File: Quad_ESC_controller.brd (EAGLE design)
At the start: 100 x 80 mm, 28 parts, among them IC1 OP-AMP, Y1 ECS-80-S-4X

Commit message: added test points
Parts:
- added J1, J2, J3, J4, J5, J6, J7, J8: (no value), SparkFun-Connectors:1X01
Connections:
- new net N$10: J1.1
- new net N$3: J4.1
- new net N$4: J5.1
- new net N$5: J6.1
- new net N$7: J7.1
- new net N$8: J3.1
- new net N$9: J2.1
- net N$6: now also J8.1
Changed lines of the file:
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@@
 <attribute name="VALUE" x="-70.485" y="3.175" size="1.27" layer="27" ratio="16" rot="R90"/>
+</element>
+<element name="J1" library="SparkFun-Connectors" library_urn="urn:adsk.eagle:library:513" package="1X01" package3d_urn="urn:adsk.eagle:package:38028/1" value="" x="-74.93" y="2.54" smashed="yes">
+<attribute name="NAME" x="-76.2" y="3.937" size="0.6096" layer="25" font="vector" ratio="20"/>
+<attribute name="VALUE" x="-76.2" y="1.016" size="0.6096" layer="27" font="vector" ratio="20" align="top-left"/>
+</element>
+<element name="J2" library="SparkFun-Connectors" library_urn="urn:adsk.eagle:library:513" package="1X01" package3d_urn="urn:adsk.eagle:package:38028/1" value="" x="-80.01" y="2.54" smashed="yes">
+<attribute name="NAME" x="-81.28" y="3.937" size="0.6096" layer="25" font="vector" ratio="20"/>
+<attribute name="VALUE" x="-81.28" y="1.016" size="0.6096" layer="27" font="vector" ratio="20" align="top-left"/>
+</element>
+<element name="J3" library="SparkFun-Connectors" library_urn="urn:adsk.eagle:library:513" package="1X01" package3d_urn="urn:adsk.eagle:package:38028/1" value="" x="-85.09" y="2.54" smashed="yes">
+<attribute name="NAME" x="-86.36" y="3.937" size="0.6096" layer="25" font="vector" ratio="20"/>
+<attribute name="VALUE" x="-86.36" y="1.016" size="0.6096" layer="27" font="vector" ratio="20" align="top-left"/>
+</element>
+<element name="J4" library="SparkFun-Connectors" library_urn="urn:adsk.eagle:library:513" package="1X01" package3d_urn="urn:adsk.eagle:package:38028/1" value="" x="-85.09" y="-2.54" smashed="yes">
+<attribute name="NAME" x="-86.36" y="-1.143" size="0.6096" layer="25" font="vector" ratio="20"/>
+<attribute name="VALUE" x="-86.36" y="-4.064" size="0.6096" layer="27" font="vector" ratio="20" align="top-left"/>
+</element>
+<element name="J5" library="SparkFun-Connectors" library_urn="urn:adsk.eagle:library:513" package="1X01" package3d_urn="urn:adsk.eagle:package:38028/1" value="" x="-81.28" y="-2.54" smashed="yes">
+<attribute name="NAME" x="-82.55" y="-1.143" size="0.6096" layer="25" font="vector" ratio="20"/>
+<attribute name="VALUE" x="-82.55" y="-4.064" size="0.6096" layer="27" font="vector" ratio="20" align="top-left"/>
+</element>
+<element name="J6" library="SparkFun-Connectors" library_urn="urn:adsk.eagle:library:513" package="1X01" package3d_urn="urn:adsk.eagle:package:38028/1" value="" x="-85.09" y="-6.35" smashed="yes">
+<attribute name="NAME" x="-86.36" y="-4.953" size="0.6096" layer="25" font="vector" ratio="20"/>
+<attribute name="VALUE" x="-86.36" y="-7.874" size="0.6096" layer="27" font="vector" ratio="20" align="top-left"/>
+</element>
+<element name="J7" library="SparkFun-Connectors" library_urn="urn:adsk.eagle:library:513" package="1X01" package3d_urn="urn:adsk.eagle:package:38028/1" value="" x="-85.09" y="-10.16" smashed="yes">
+<attribute name="NAME" x="-86.36" y="-8.763" size="0.6096" layer="25" font="vector" ratio="20"/>
+<attribute name="VALUE" x="-86.36" y="-11.684" size="0.6096" layer="27" font="vector" ratio="20" align="top-left"/>
+</element>
+<element name="J8" library="SparkFun-Connectors" library_urn="urn:adsk.eagle:library:513" package="1X01" package3d_urn="urn:adsk.eagle:package:38028/1" value="" x="-90.17" y="-8.89" smashed="yes">
+<attribute name="NAME" x="-91.44" y="-7.493" size="0.6096" layer="25" font="vector" ratio="20"/>
+<attribute name="VALUE" x="-91.44" y="-10.414" size="0.6096" layer="27" font="vector" ratio="20" align="top-left"/>
 </element>
 </elements>
@@
 <contactref element="R6" pad="1"/>
 <contactref element="OP-AMP1" pad="2"/>
+<contactref element="J8" pad="1"/>
+<wire x1="-59.055" y1="2.2225" x2="-90.17" y2="-8.89" width="0" layer="19" extent="1-1"/>
 <wire x1="-44.87" y1="67.31" x2="-59.055" y2="2.2225" width="0" layer="19" extent="1-1"/>
 <wire x1="-38.95" y1="67.31" x2="-44.87" y2="67.31" width="0" layer="19" extent="1-1"/>
 </signal>
+<signal name="N$3">
+<contactref element="J4" pad="1"/>
+</signal>
+<signal name="N$4">
+<contactref element="J5" pad="1"/>
+</signal>
+<signal name="N$5">
+<contactref element="J6" pad="1"/>
+</signal>
+<signal name="N$7">
+<contactref element="J7" pad="1"/>
+</signal>
+<signal name="N$8">
+<contactref element="J3" pad="1"/>
+</signal>
+<signal name="N$9">
+<contactref element="J2" pad="1"/>
+</signal>
+<signal name="N$10">
+<contactref element="J1" pad="1"/>
+</signal>
 </signals>

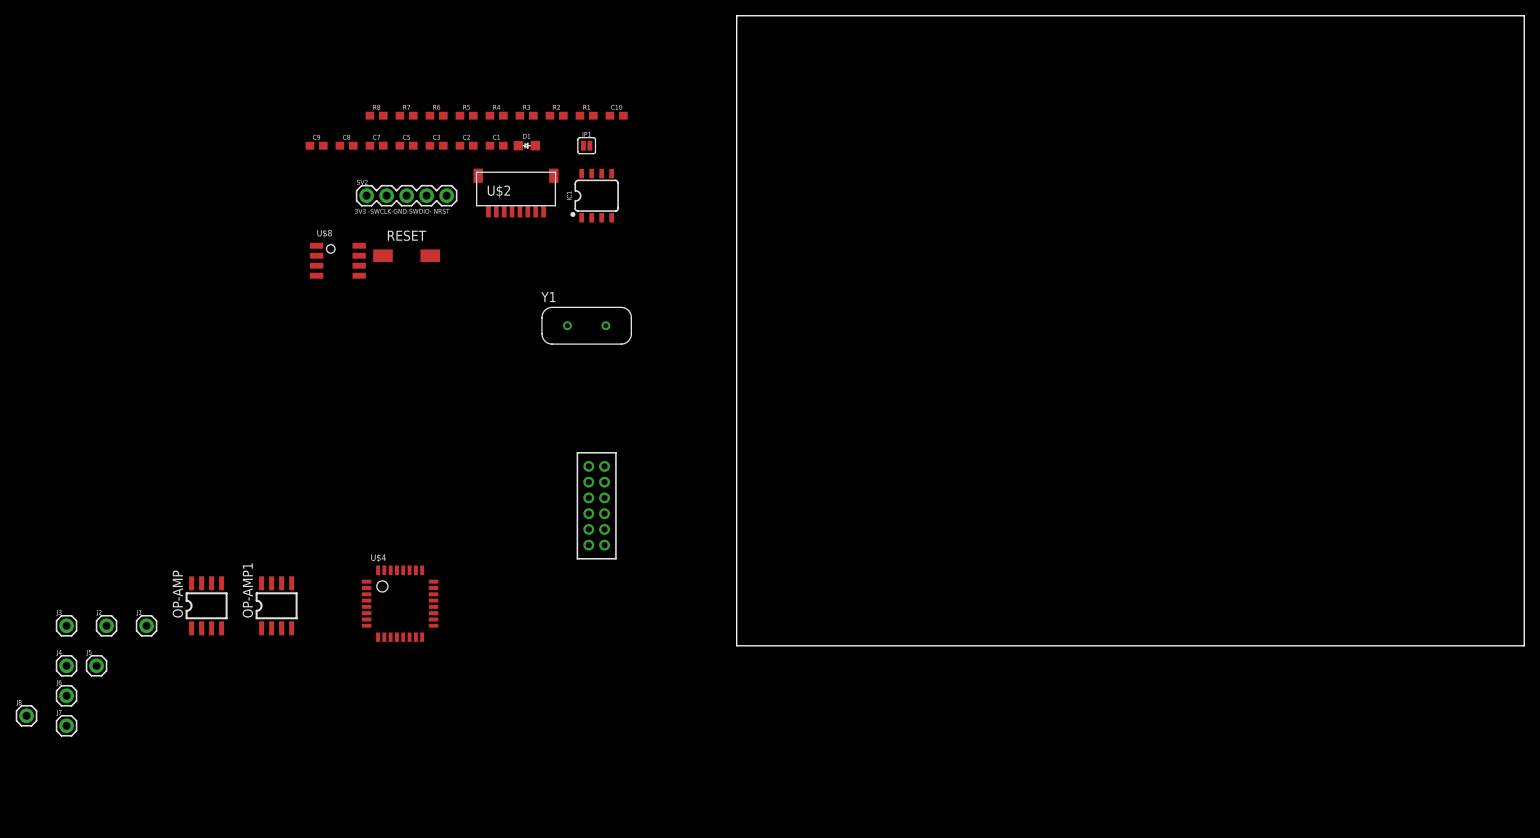
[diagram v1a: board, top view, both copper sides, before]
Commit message: add board size
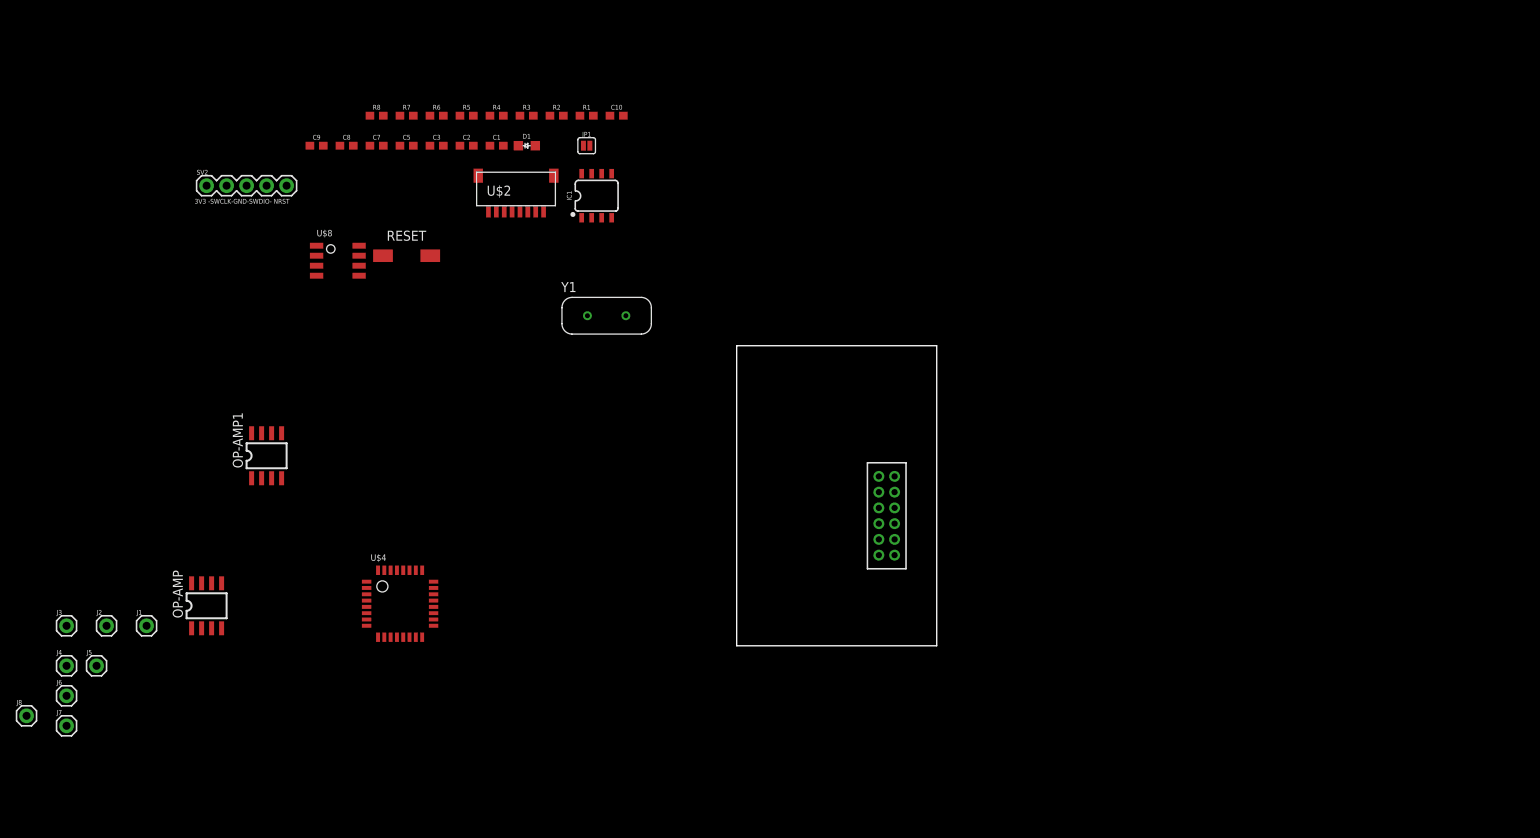
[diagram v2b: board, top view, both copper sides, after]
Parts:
- moved U$3 36.9 mm to (19.1, 16.5)
- moved SV2 20.4 mm to (-67.3, 58.4)
- moved OP-AMP1 19.1 mm to (-59.7, 24.1)
- moved Y1 2.84 mm to (-16.5, 41.9)
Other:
- board size 100 x 80 mm -> 25.4 x 38.1 mm

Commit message: Example placement for adapter
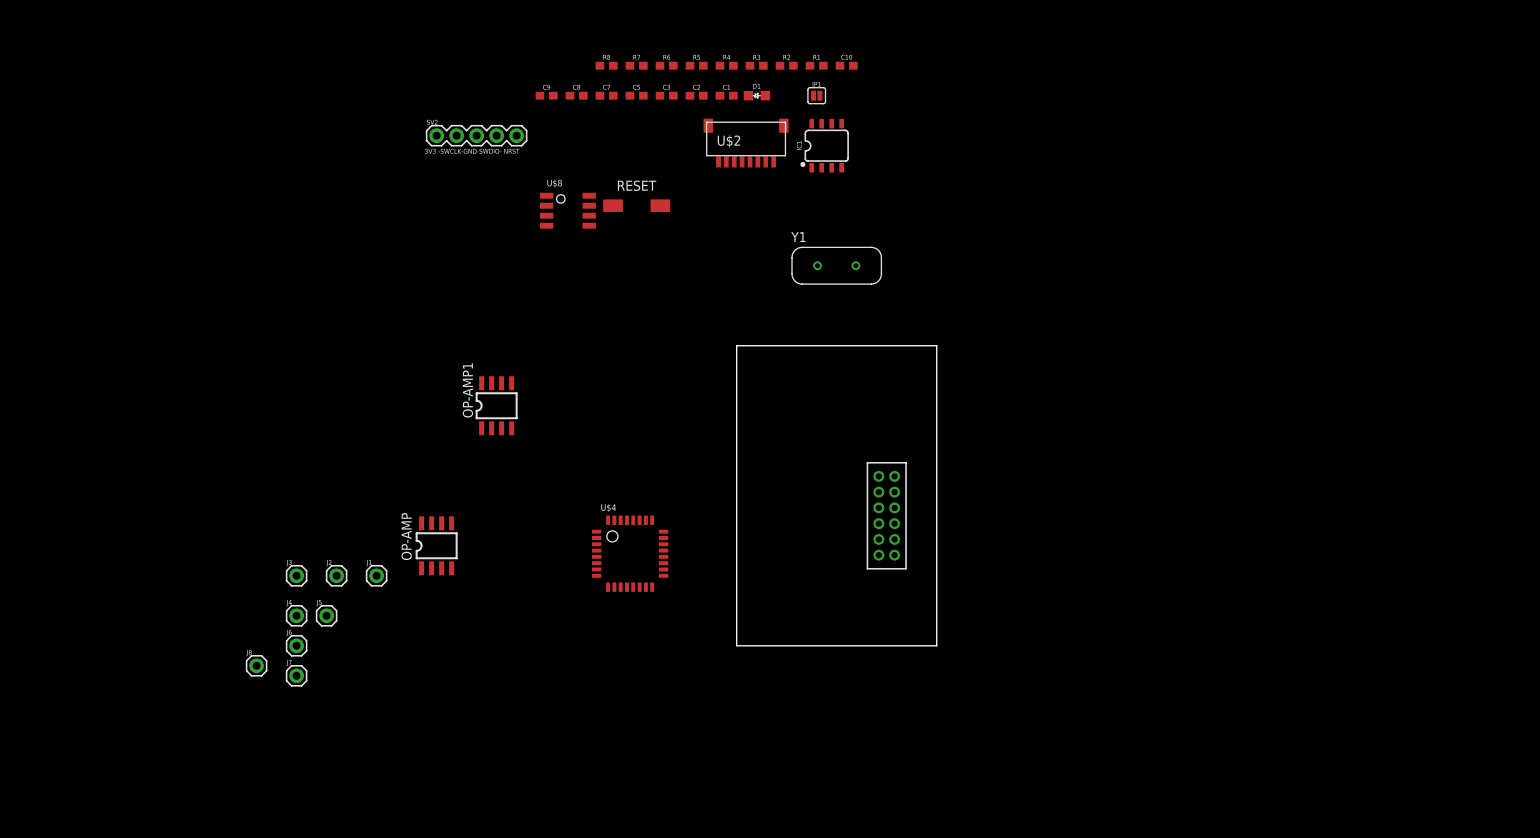
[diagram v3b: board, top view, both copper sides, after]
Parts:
- moved OP-AMP 30.2 mm to (-38.1, 12.7)
- moved J1 29.9 mm to (-45.7, 8.89)
- moved J2 29.9 mm to (-50.8, 8.89)
- moved C9 29.9 mm to (-24.1, 69.8)
- moved U$2 29.9 mm to (-3.81, 62.2)
- moved U$8 29.9 mm to (-24.1, 53.3)
- moved C1 29.9 mm to (-1.27, 69.8)
- moved C10 29.9 mm to (14.0, 73.7)
- moved C2 29.9 mm to (-5.08, 69.8)
- moved C3 29.9 mm to (-8.89, 69.8)
- moved C8 29.9 mm to (-20.3, 69.8)
- moved D1 29.9 mm to (2.54, 69.8)
- moved IC1 29.9 mm to (11.4, 63.5)
- moved J3 29.9 mm to (-55.9, 8.89)
- moved J4 29.9 mm to (-55.9, 3.81)
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
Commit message: moved stuff around
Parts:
- moved U$8 65.1 mm to (16.5, 2.47)
- moved U$2 61.6 mm to (5.32, 1.28), turned to 90 degrees
- moved IC1 59.7 mm to (11.0, 3.81), flipped to the bottom, turned to 90 degrees
- moved OP-AMP 59.4 mm to (13.7, 41.8), turned to 270 degrees
- moved SV2 56.5 mm to (7.42, 31.4)
- moved OP-AMP1 53.9 mm to (22.0, 42.7), turned to 270 degrees
- moved RESET 30.9 mm to (2.66, 29.1), turned to 90 degrees
- moved U$4 23.8 mm to (5.86, 11.9)
- moved Y1 22.8 mm to (10.8, 25.5)

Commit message: moved stuff around
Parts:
- moved C5 74.2 mm to (31.0, 9.88)
- moved R8 70.6 mm to (4.96, 6.46), turned to 90 degrees
- moved C3 70.2 mm to (31.1, 12.2)
- moved C1 69.1 mm to (44.5, 18.1), turned to 90 degrees
- moved R6 69.0 mm to (6.72, 6.43), turned to 270 degrees
- moved R5 68.5 mm to (8.41, 6.47), turned to 270 degrees
- moved R2 67.9 mm to (2.51, 5.86), flipped to the bottom, turned to 180 degrees
- moved C2 67.1 mm to (32.0, 13.9)
- moved C7 66.8 mm to (2.50, 5.82)
- moved JP1 61.2 mm to (16.4, 8.99)
- moved C9 57.6 mm to (16.5, 29.1), turned to 180 degrees
- moved R4 55.5 mm to (1.55, 18.2), flipped to the bottom, turned to 90 degrees
- moved R7 51.7 mm to (9.84, 27.1)
- moved C8 51.0 mm to (16.8, 34.9), turned to 90 degrees
- moved D1 49.2 mm to (36.6, 34.3)
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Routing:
- added copper zone on layer 1, net GND
- added copper zone on layer 16, net GND

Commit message: Routed some ish
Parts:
- moved J1 59.5 mm to (11.2, -8.38)
- moved J2 59.5 mm to (6.10, -8.38)
- moved J4 59.5 mm to (1.02, -13.5)
- moved J5 59.5 mm to (4.83, -13.5)
- moved J6 59.5 mm to (1.02, -17.3)
- moved J7 59.5 mm to (1.02, -21.1)
- moved J8 59.5 mm to (-4.06, -19.8)
- moved J3 57.0 mm to (-4.32, -15.5)
- moved C1 43.1 mm to (1.56, 21.7)
- moved D1 31.4 mm to (6.07, 27.0)
- moved C10 30.4 mm to (2.20, 25.4), turned to 90 degrees
- moved C5 23.8 mm to (12.7, 25.2), turned to 180 degrees
- moved C2 19.9 mm to (14.1, 22.6), turned to 90 degrees
- moved C3 18.5 mm to (14.0, 19.1), turned to 90 degrees
- moved R2 1.52 mm to (2.51, 7.38)
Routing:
- net +3V3: track 0.00 -> 86.5 mm, vias 0 -> 4
- net TLM: track 0.00 -> 30.4 mm, vias 0 -> 3
- net TLM_ESC: track 0.00 -> 11.9 mm, vias 0 -> 1
- net N$2: track 0.00 -> 6.99 mm
- net N$1: track 0.00 -> 5.69 mm
- net N$6: track 0.00 -> 4.93 mm, vias 0 -> 1
- net LED: track 0.00 -> 2.55 mm
- net N$24: track 0.00 -> 1.89 mm

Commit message: routed airwires
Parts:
- moved C1 0.84 mm to (1.53, 22.5)
- moved C3 0.80 mm to (14.7, 19.4)
- moved C2 0.78 mm to (14.8, 22.8)
- moved R2 0.76 mm to (2.51, 8.15)
- moved C10 0.57 mm to (1.95, 25.9)
- moved U$4 0.25 mm to (3.87, 17.5)
- moved R6 0.24 mm to (6.92, 6.56)
- moved R8 0.13 mm to (4.89, 6.56)
- moved R4 0.08 mm to (1.52, 18.1)
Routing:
- net NRST: track 0.00 -> 76.3 mm, vias 0 -> 5
- net CAN_L: track 0.00 -> 34.2 mm, vias 0 -> 2
- net ESC_ID: track 0.00 -> 31.0 mm, vias 0 -> 2
- net CAN_H: track 0.00 -> 28.3 mm
- net SWCLK: track 0.00 -> 23.8 mm, vias 0 -> 1
- net SWDIO: track 0.00 -> 23.4 mm, vias 0 -> 2
- net OSC_IN: track 0.00 -> 17.9 mm, vias 0 -> 2
- net OSC_OUT: track 0.00 -> 15.9 mm, vias 0 -> 2
- net +3V3: track 86.5 -> 100.9 mm, vias 4 -> 5
- net TIM3_CH4: track 0.00 -> 7.86 mm
- net TIM3_CH3: track 0.00 -> 7.78 mm
- net TIM3_CH2: track 0.00 -> 7.69 mm
- net TIM3_CH1: track 0.00 -> 7.61 mm
- net ADC: track 0.00 -> 7.45 mm
- net CAN_RX: track 0.00 -> 5.79 mm, vias 0 -> 1
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
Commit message: made test points nice
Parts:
- removed J4, J5: (no value), SparkFun-Connectors:1X01
- added J10, J11: (no value), SparkFun-Connectors:1X01
- moved J8 26.4 mm to (11.4, 1.52)
- moved J7 22.3 mm to (-19.6, -12.4)
- moved J6 17.2 mm to (-15.5, -12.4)
- moved J1 15.0 mm to (-3.30, -12.4)
- moved J2 14.1 mm to (-7.37, -12.4)
- moved J3 7.74 mm to (-11.4, -12.4)
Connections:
- removed net N$10: J1.1
- removed net N$3: J4.1
- removed net N$4: J5.1
- removed net N$5: J6.1
- removed net N$7: J7.1
- removed net N$8: J3.1
- removed net N$9: J2.1
- net CAN_H: now also J10.1
- net CAN_L: now also J11.1
- net CAN_RX: now also J7.1
- net CAN_TX: now also J6.1
- net NRST: now also J3.1
- net SWCLK: now also J1.1
- net SWDIO: now also J2.1
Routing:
- net +3V3: track 100.9 -> 104.7 mm, vias 5 -> 6
- net ESC_ID: track 31.0 -> 28.3 mm
